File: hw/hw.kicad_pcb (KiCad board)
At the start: 2 copper layers, 25 parts, among them J1 Motor 1 Connector, J2 Motor 2 Connector, J3 Distance sensor 3, J4 Distance sensor 1, J5 Distance sensor 2, J6 Distance sensor 6, J7 Distance sensor 4, J8 Distance sensor 5, U1 TB6612FNG_Breakout, U2 74HC595

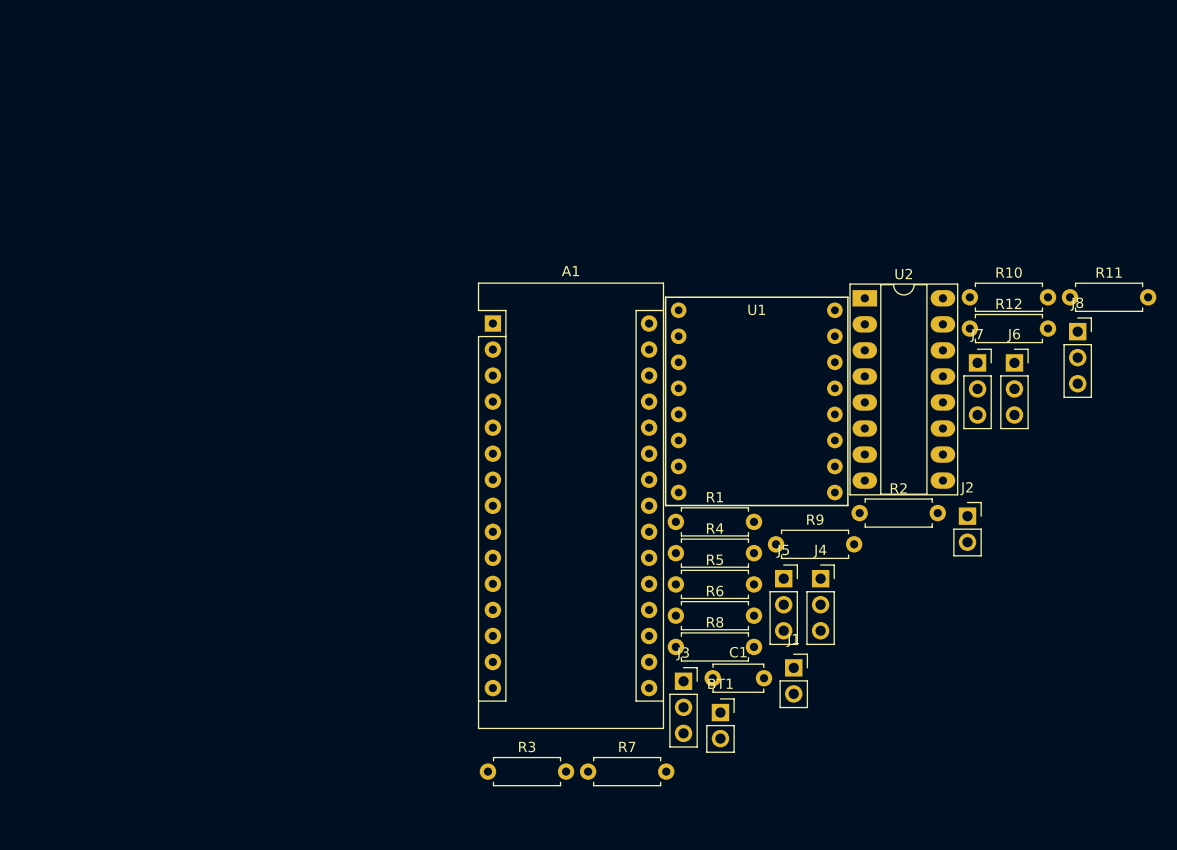
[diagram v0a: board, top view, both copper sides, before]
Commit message: Laid out PCB footprints
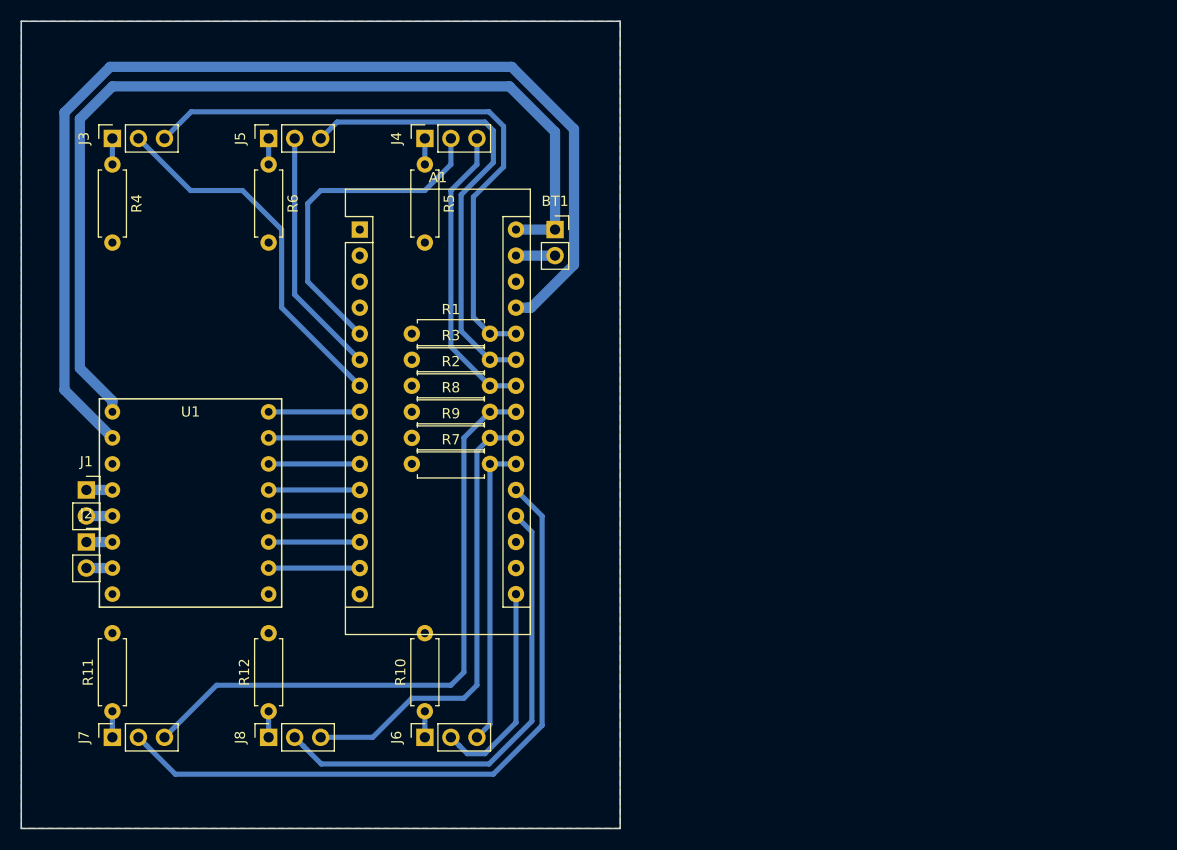
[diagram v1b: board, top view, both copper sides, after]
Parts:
- removed C1: 100n, Capacitor_THT:C_Disc_D4.7mm_W2.5mm_P5.00mm
- removed U2: 74HC595, Package_DIP:DIP-16_W7.62mm_Socket_LongPads
- moved R11 101.8 mm to (87.6, 115.6), turned to 90 degrees
- moved J7 92.0 mm to (87.6, 118.1), turned to 90 degrees
- moved J8 88.3 mm to (102.9, 118.1), turned to 90 degrees
- moved J2 86.0 mm to (85.1, 99.1)
- moved R12 77.9 mm to (102.9, 115.6), turned to 90 degrees
- moved J3 76.9 mm to (87.6, 59.7), turned to 90 degrees
- moved J1 71.2 mm to (85.1, 94.0)
- moved J6 68.1 mm to (118.1, 118.1), turned to 90 degrees
- moved R4 66.8 mm to (87.6, 62.2), turned to 270 degrees
- moved R10 66.8 mm to (118.1, 115.6), turned to 90 degrees
- moved J5 66.1 mm to (102.9, 59.7), turned to 90 degrees
- moved R6 59.3 mm to (102.9, 62.2), turned to 270 degrees
- moved J4 57.7 mm to (118.1, 59.7), turned to 90 degrees
- moved U1 56.1 mm to (95.2, 83.8)
- moved BT1 49.8 mm to (130.8, 68.6)
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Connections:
- A1 pad 10: dist-led-6 -> Net-(A1-Pad10)
- A1 pad 11: 595-latch -> Net-(A1-Pad11)
- A1 pad 12: PWMA -> Net-(A1-Pad12)
- A1 pad 13: PWMB -> Net-(A1-Pad13)
- A1 pad 14: 595-data -> Net-(A1-Pad14)
- A1 pad 15: 595-clock -> Net-(A1-Pad15)
- A1 pad 16: motor-stby -> dist-led-6
- A1 pad 19: dist-sig-1 -> dist-led-5
- A1 pad 20: dist-sig-2 -> dist-led-4
- A1 pad 21: dist-sig-3 -> dist-sig-6
- A1 pad 22: dist-sig-4 -> dist-sig-5
- A1 pad 23: dist-sig-5 -> dist-sig-4
- A1 pad 24: dist-sig-6 -> dist-sig-1
- A1 pad 25: Net-(A1-Pad25) -> dist-sig-2
- A1 pad 26: Net-(A1-Pad26) -> dist-sig-3
- A1 pad 4: Net-(A1-Pad4) -> GND
- A1 pad 8: dist-led-4 -> Net-(A1-Pad8)
- A1 pad 9: dist-led-5 -> Net-(A1-Pad9)
- U1 pad 10: PWMB -> Net-(A1-Pad14)
- U1 pad 11: Net-(U1-Pad11) -> Net-(A1-Pad13)
- U1 pad 12: Net-(U1-Pad12) -> Net-(A1-Pad12)
- U1 pad 13: motor-stby -> Net-(A1-Pad11)
- U1 pad 14: Net-(U1-Pad14) -> Net-(A1-Pad10)
- U1 pad 15: Net-(U1-Pad15) -> Net-(A1-Pad9)
- U1 pad 16: PWMA -> Net-(A1-Pad8)
- U1 pad 9: Net-(U1-Pad9) -> GND
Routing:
- net +5V: track 0.00 -> 108.4 mm
- net +9V: track 0.00 -> 92.7 mm
- net dist-led-4: track 0.00 -> 66.9 mm
- net dist-sig-4: track 0.00 -> 60.8 mm
- net dist-sig-3: track 0.00 -> 59.4 mm
- net dist-led-5: track 0.00 -> 46.6 mm
- net dist-sig-2: track 0.00 -> 45.2 mm
- net dist-sig-5: track 0.00 -> 44.5 mm
- net dist-led-3: track 0.00 -> 36.0 mm
- net dist-led-1: track 0.00 -> 32.9 mm
- net dist-sig-6: track 0.00 -> 29.7 mm
- net dist-sig-1: track 0.00 -> 29.3 mm
- net dist-led-2: track 0.00 -> 24.2 mm
- net dist-led-6: track 0.00 -> 20.8 mm
- net Net-(A1-Pad9): track 0.00 -> 8.89 mm
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- added copper zone on B.Cu, net GND
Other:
- board outline added: 58.4 x 78.7 mm
- net class Default: clearance 0.2 -> 0.5; trace_width 0.25 -> 0.5; via_dia 0.8 -> 1.5; via_drill 0.4 -> 0.8
- rule trace_clearance: 0.2 -> 0.5
- rule via_min_drill: 0.3 -> 0.8
- rule via_min_size: 0.4 -> 0.8

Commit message: new pcb version
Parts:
- removed R11, R12: 56, Resistor_THT:R_Axial_DIN0207_L6.3mm_D2.5mm_P7.62mm_Horizontal
- added C1: 100u, Capacitor_THT:CP_Radial_D6.3mm_P2.50mm, F.Cu at (116.2, 92.7)
- added C2: 100n, Capacitor_SMD:C_0805_2012Metric_Pad1.15x1.40mm_HandSolder, B.Cu at (124.2, 115.6)
- added C3: 100n, Capacitor_SMD:C_0805_2012Metric_Pad1.15x1.40mm_HandSolder, B.Cu at (120.7, 59.4)
- added C4: 100n, Capacitor_SMD:C_0805_2012Metric_Pad1.15x1.40mm_HandSolder, B.Cu at (104.8, 59.4)
- added C5: 100n, Capacitor_SMD:C_0805_2012Metric_Pad1.15x1.40mm_HandSolder, B.Cu at (88.3, 59.4)
- added C6: 100n, Capacitor_SMD:C_0805_2012Metric_Pad1.15x1.40mm_HandSolder, B.Cu at (113.0, 112.0)
- added C7: 100n, Capacitor_SMD:C_0805_2012Metric_Pad1.15x1.40mm_HandSolder, B.Cu at (118.1, 112.0)
- added D1: 1N5817, Diode_THT:D_DO-41_SOD81_P7.62mm_Horizontal, F.Cu at (116.2, 87.0)
- added REF**: R_Axial_DIN0207_L6.3mm_D2.5mm_P10.16mm_Horizontal, Resistor_THT:R_Axial_DIN0207_L6.3mm_D2.5mm_P10.16mm_Horizontal, F.Cu at (81.9, 114.3)
- added REF**: R_Axial_DIN0207_L6.3mm_D2.5mm_P10.16mm_Horizontal, Resistor_THT:R_Axial_DIN0207_L6.3mm_D2.5mm_P10.16mm_Horizontal, F.Cu at (114.3, 71.1)
- added REF**: R_Axial_DIN0207_L6.3mm_D2.5mm_P10.16mm_Horizontal, Resistor_THT:R_Axial_DIN0207_L6.3mm_D2.5mm_P10.16mm_Horizontal, F.Cu at (98.4, 71.1)
- added REF**: R_Axial_DIN0207_L6.3mm_D2.5mm_P10.16mm_Horizontal, Resistor_THT:R_Axial_DIN0207_L6.3mm_D2.5mm_P10.16mm_Horizontal, F.Cu at (87.6, 114.3)
- added REF**: R_Axial_DIN0207_L6.3mm_D2.5mm_P10.16mm_Horizontal, Resistor_THT:R_Axial_DIN0207_L6.3mm_D2.5mm_P10.16mm_Horizontal, F.Cu at (124.5, 109.9)
- added U2: L3GD20_breakout, custom:L3GD20_breakout, F.Cu at (108.0, 67.9)
- J3: value Distance sensor 3 -> Distance sensor 2
- J5: value Distance sensor 2 -> Distance sensor 3
- J6: value Distance sensor 6 -> Serial pin header; footprint Connector_PinSocket_2.54mm:PinSocket_1x03_P2.54mm_Vertical -> Connector_PinHeader_2.54mm:PinHeader_1x02_P2.54mm_Vertical
- R1, R2, R3, R7, R9: value 100k -> 1M; footprint Resistor_THT:R_Axial_DIN0207_L6.3mm_D2.5mm_P7.62mm_Horizontal -> Resistor_SMD:R_0805_2012Metric_Pad1.15x1.40mm_HandSolder; moved to B.Cu
- R10, R4, R5, R6: value 56 -> 330; footprint Resistor_THT:R_Axial_DIN0207_L6.3mm_D2.5mm_P7.62mm_Horizontal -> Resistor_SMD:R_0805_2012Metric_Pad1.15x1.40mm_HandSolder; moved to B.Cu
- R8: value 100k -> 330; footprint Resistor_THT:R_Axial_DIN0207_L6.3mm_D2.5mm_P7.62mm_Horizontal -> Resistor_SMD:R_0805_2012Metric_Pad1.15x1.40mm_HandSolder; moved to B.Cu
- moved R8 44.8 mm to (92.3, 123.8), turned to 180 degrees
- moved A1 38.2 mm to (125.7, 104.1), turned to 270 degrees
- moved R3 37.5 mm to (86.4, 59.4), turned to 90 degrees
- moved R2 24.6 mm to (118.1, 59.3), turned to 90 degrees
- moved R1 24.2 mm to (102.2, 59.4), turned to 90 degrees
- moved J3 23.4 mm to (110.5, 54.6), turned to 270 degrees
- moved R9 23.1 mm to (115.6, 112.0), turned to 270 degrees
- moved R4 23.0 mm to (110.5, 59.4)
- moved R7 21.5 mm to (110.5, 112.0), turned to 270 degrees
- moved J2 19.4 mm to (95.2, 82.5), turned to 270 degrees
- moved J1 19.1 mm to (100.3, 82.5), turned to 270 degrees
- moved BT1 18.9 mm to (126.4, 87.0)
- moved J6 18.5 mm to (123.2, 100.3)
- moved U1 17.6 mm to (110.5, 92.7), turned to 270 degrees
- moved J8 13.7 mm to (115.6, 123.2)
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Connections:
- A1 pad 15: Net-(A1-Pad15) -> dist-led-4
- A1 pad 16: dist-led-6 -> dist-led-5
- A1 pad 19: dist-led-5 -> dist-sig-1
- A1 pad 20: dist-led-4 -> dist-sig-2
- A1 pad 21: dist-sig-6 -> dist-sig-3
- A1 pad 22: dist-sig-5 -> Net-(A1-Pad22)
- A1 pad 23: dist-sig-4 -> IMU_SDA
- A1 pad 24: dist-sig-1 -> IMU_SCL
- A1 pad 25: dist-sig-2 -> dist-sig-4
- A1 pad 26: dist-sig-3 -> dist-sig-5
- A1 pad 30: +9V -> V_a
- J3 pad 2: dist-led-3 -> dist-led-2
- J3 pad 3: dist-sig-3 -> dist-sig-2
- J5 pad 2: dist-led-2 -> dist-led-3
- J5 pad 3: dist-sig-2 -> dist-sig-3
- J6 pad 1: Net-(J6-Pad1) -> Net-(A1-Pad2)
- J6 pad 2: dist-led-6 -> Net-(A1-Pad1)
- R1 pad 2: dist-sig-3 -> dist-sig-2
- R10 pad 1: Net-(J6-Pad1) -> Net-(J8-Pad1)
- R3 pad 2: dist-sig-2 -> dist-sig-3
- R7 pad 2: dist-sig-6 -> dist-sig-4
- R8 pad 1: GND -> Net-(J7-Pad1)
- R8 pad 2: dist-sig-4 -> GND
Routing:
- net IMU_SCL: track 0.00 -> 91.0 mm
- net IMU_SDA: track 0.00 -> 90.3 mm
- net dist-sig-1: track 29.3 -> 119.3 mm
- net +9V: track 92.7 -> 22.6 mm
- net dist-led-1: track 32.9 -> 102.3 mm
- net dist-led-2: track 24.2 -> 89.3 mm
- net dist-sig-2: track 45.2 -> 103.1 mm
- net V_a: track 0.00 -> 48.6 mm
- net dist-led-3: track 36.0 -> 74.8 mm
- net dist-sig-4: track 60.8 -> 23.4 mm
- net dist-led-4: track 66.9 -> 29.9 mm
- net dist-sig-3: track 59.4 -> 89.2 mm
- net dist-sig-6: track 29.7 -> 0.00 mm
- net dist-sig-5: track 44.5 -> 15.5 mm
- net dist-led-6: track 20.8 -> 0.00 mm
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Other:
- net class Default: clearance 0.5 -> 0.3
- rule trace_clearance: 0.5 -> 0.3

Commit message: Added PCB v1.2
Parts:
- removed REF** (x5): R_Axial_DIN0207_L6.3mm_D2.5mm_P10.16mm_Horizontal, Resistor_THT:R_Axial_DIN0207_L6.3mm_D2.5mm_P10.16mm_Horizontal
- added 5V: , Connector_PinHeader_2.54mm:PinHeader_1x01_P2.54mm_Vertical, F.Cu at (105.4, 78.7)
- added ?: , Connector_PinHeader_2.54mm:PinHeader_1x01_P2.54mm_Vertical, F.Cu at (130.8, 75.6)
- added ?: , TestPoint:TestPoint_Plated_Hole_D3.0mm, F.Cu at (82.4, 122.8)
- added ?: , TestPoint:TestPoint_Plated_Hole_D3.0mm, F.Cu at (133.5, 122.8)
- added ?: , TestPoint:TestPoint_Plated_Hole_D3.0mm, F.Cu at (133.5, 52.4)
- added ?: , TestPoint:TestPoint_Plated_Hole_D3.0mm, F.Cu at (82.4, 52.4)
- added ?: , Connector_PinHeader_2.54mm:PinHeader_1x10_P2.54mm_Vertical, F.Cu at (96.5, 71.1)
- added ?: , Connector_PinHeader_2.54mm:PinHeader_1x01_P2.54mm_Vertical, F.Cu at (130.8, 88.9)
- added TP1: , TestPoint:TestPoint_Pad_D2.0mm, F.Cu at (99.7, 50.8)
- added TP2: , TestPoint:TestPoint_Pad_D2.0mm, F.Cu at (113.7, 50.8)
- added TP3: , TestPoint:TestPoint_Pad_D2.0mm, F.Cu at (127.6, 50.8)
- added TP4: , TestPoint:TestPoint_Pad_D2.0mm, F.Cu at (95.2, 121.3)
- added TP5: , TestPoint:TestPoint_Pad_D2.0mm, F.Cu at (125.7, 121.3)
- BT1: value Battery_Cell -> Battery
- C2, C3, C4, C5, C6, C7, R1, R10, R2, R3, R4, R5, R6, R7, R8, R9: moved to F.Cu
- J1: value Motor 1 Connector -> M1
- J2: value Motor 2 Connector -> M2
- J3: value Distance sensor 2 -> sensor 2
- J4: value Distance sensor 1 -> sensor 1
- J5: value Distance sensor 3 -> sensor 3
- J6: value Serial pin header -> TX/RX
- J7: value Distance sensor 4 -> sensor 4
- J8: value Distance sensor 5 -> sensor 5
- moved C5 38.8 mm to (127.0, 56.9)
- moved R3 38.2 mm to (124.5, 56.9)
- moved J4 35.8 mm to (91.4, 50.8), turned to 90 degrees
- moved R5 35.7 mm to (91.4, 56.9)
- moved R6 25.5 mm to (119.4, 56.9)
- moved J5 23.2 mm to (119.4, 50.8), turned to 90 degrees
- moved C3 21.7 mm to (99.1, 56.9)
- moved R2 21.7 mm to (96.5, 56.9)
- moved R10 9.75 mm to (120.7, 120.4), turned to 90 degrees
- moved C4 8.64 mm to (113.0, 56.9)
- moved R1 8.64 mm to (110.5, 56.9)
- moved BT1 7.24 mm to (130.8, 81.3)
- moved D1 7.24 mm to (120.7, 81.3)
- moved C1 6.75 mm to (120.7, 87.6)
- moved J3 6.35 mm to (105.4, 50.8), turned to 90 degrees
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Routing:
- net GND: track 3.81 -> 53.9 mm
- net IMU_SDA: track 90.3 -> 49.4 mm, vias 0 -> 1
- net IMU_SCL: track 91.0 -> 51.5 mm
- net dist-sig-1: track 119.3 -> 86.6 mm
- net dist-sig-3: track 89.2 -> 117.3 mm, vias 0 -> 2
- net dist-led-2: track 89.3 -> 63.2 mm, vias 0 -> 1
- net +5V: track 110.9 -> 85.0 mm
- net dist-led-3: track 74.8 -> 56.6 mm
- net +9V: track 22.6 -> 32.3 mm
- net dist-sig-5: track 15.5 -> 22.2 mm
- net V_a: track 48.6 -> 42.4 mm
- net dist-sig-4: track 23.4 -> 29.4 mm
- net dist-led-1: track 102.3 -> 97.1 mm, vias 0 -> 2
- net dist-led-4: track 29.9 -> 24.9 mm, vias 0 -> 1
- net dist-led-5: track 40.5 -> 36.2 mm, vias 0 -> 2
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- added copper zone on F.Cu, net GND
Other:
- net class Default: trace_width 0.5 -> 0.3; via_dia 1.5 -> 0.7; via_drill 0.8 -> 0.3
- rule trace_min: 0.2 -> 0.25
- rule via_min_drill: 0.8 -> 0.2
- rule via_min_size: 0.8 -> 0.6
- board text added: "+"
- board text added: "9V"
- board text added: "Arduino Nano"
- board text added: "GND"
- board text added: "LSM303DLHC"
- board text added: "Mazeblazer v1.2"
- board text added: "Probe GND"
- board text added: "TB6612FNG"
